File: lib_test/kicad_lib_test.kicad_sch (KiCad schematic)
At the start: 0 parts

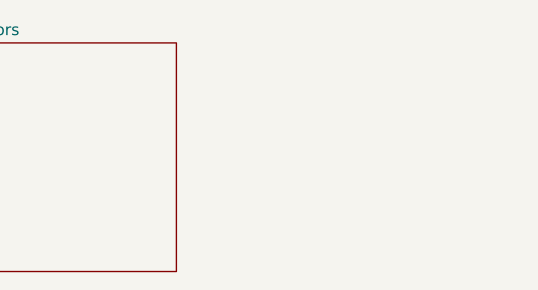
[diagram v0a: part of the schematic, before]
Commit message: add capacitors series to test project
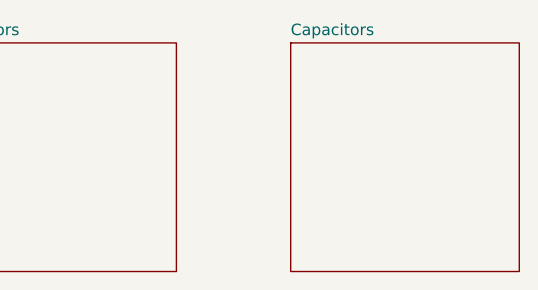
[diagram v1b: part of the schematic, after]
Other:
- added sheet Capacitors (capacitors.kicad_sch)
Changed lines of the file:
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@@
+	)
+	(sheet
+		(at 63.5 25.4)
+		(size 25.4 25.4)
+		(fields_autoplaced yes)
+		(stroke
+			(width 0.1524)
+			(type solid)
+		)
+		(fill
+			(color 0 0 0 0.0000)
+		)
+		(property "Sheetname" "Capacitors"
+			(at 63.5 24.6884 0)
+			(effects
+				(font
+					(size 1.27 1.27)
+				)
+				(justify left bottom)
+			)
+		)
+		(property "Sheetfile" "capacitors.kicad_sch"
+			(at 63.5 51.3846 0)
+			(effects
+				(font
+					(size 1.27 1.27)
+				)
+				(justify left top)
+				(hide yes)
+			)
+		)
+		(instances
+			(project "kicad_lib_test"
+				(path "/032b8f2d-5c08-4381-9e3a-c197ca84e3c5"
+					(page "3")
+				)
+			)
+		)
 	)
 	(sheet

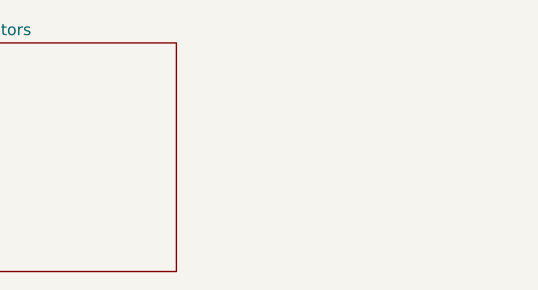
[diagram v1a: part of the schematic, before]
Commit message: add inductor bead 600R, 1.5A, 0.25R
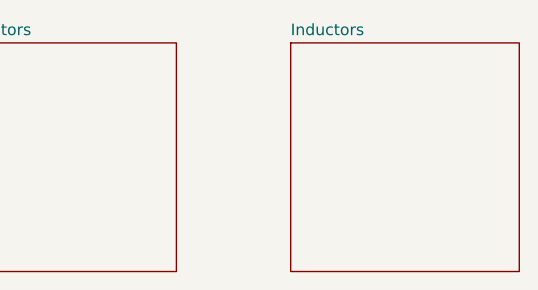
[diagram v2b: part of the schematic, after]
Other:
- added sheet Inductors (inductors.kicad_sch)
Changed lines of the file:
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@@
+		)
+	)
+	(sheet
+		(at 101.6 25.4)
+		(size 25.4 25.4)
+		(fields_autoplaced yes)
+		(stroke
+			(width 0.1524)
+			(type solid)
+		)
+		(fill
+			(color 0 0 0 0.0000)
+		)
+		(property "Sheetname" "Inductors"
+			(at 101.6 24.6884 0)
+			(effects
+				(font
+					(size 1.27 1.27)
+				)
+				(justify left bottom)
+			)
+		)
+		(property "Sheetfile" "inductors.kicad_sch"
+			(at 101.6 51.3846 0)
+			(effects
+				(font
+					(size 1.27 1.27)
+				)
+				(justify left top)
+				(hide yes)
+			)
+		)
+		(instances
+			(project "kicad_lib_test"
+				(path "/032b8f2d-5c08-4381-9e3a-c197ca84e3c5"
+					(page "4")
+				)
+			)
 		)
 	)

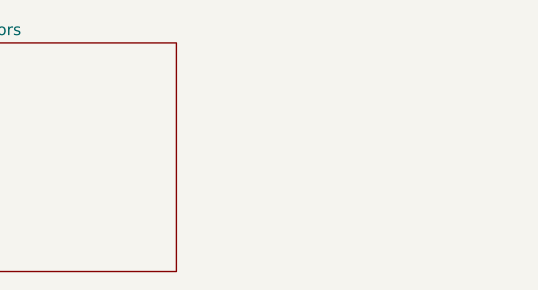
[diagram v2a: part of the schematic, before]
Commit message: add diode tvs uni 2 channel 12V
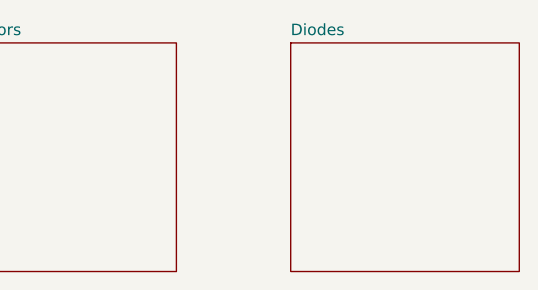
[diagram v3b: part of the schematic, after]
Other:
- added sheet Diodes (diodes.kicad_sch)
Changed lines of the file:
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@@
 	(title_block
 		(title "Lily KiCad Library test")
-		(date "2024-04-17")
+		(date "2024-04-28")
 		(rev "1")
 		(company "LilyTronics")
@@
 				)
 			)
+		)
+	)
+	(sheet
+		(at 139.7 25.4)
+		(size 25.4 25.4)
+		(fields_autoplaced yes)
+		(stroke
+			(width 0.1524)
+			(type solid)
+		)
+		(fill
+			(color 0 0 0 0.0000)
+		)
+		(property "Sheetname" "Diodes"
+			(at 139.7 24.6884 0)
+			(effects
+				(font
+					(size 1.27 1.27)
+				)
+				(justify left bottom)
+			)
+		)
+		(property "Sheetfile" "diodes.kicad_sch"
+			(at 139.7 51.3846 0)
+			(effects
+				(font
+					(size 1.27 1.27)
+				)
+				(justify left top)
+				(hide yes)
+			)
+		)
+		(instances
+			(project "kicad_lib_test"
+				(path "/032b8f2d-5c08-4381-9e3a-c197ca84e3c5"
+					(page "5")
+				)
+			)

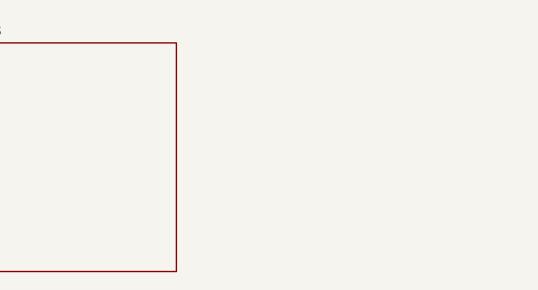
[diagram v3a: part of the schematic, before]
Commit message: add MOSFET AO3400A
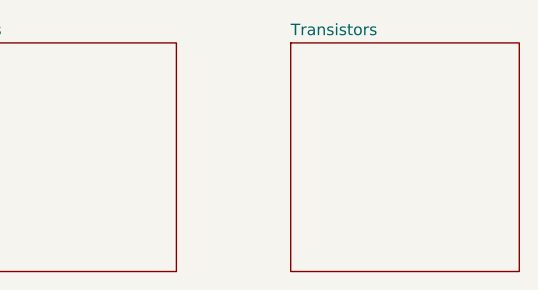
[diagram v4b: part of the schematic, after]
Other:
- added sheet Transistors (transistors.kicad_sch)
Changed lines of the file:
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@@
+	)
+	(sheet
+		(at 177.8 25.4)
+		(size 25.4 25.4)
+		(fields_autoplaced yes)
+		(stroke
+			(width 0.1524)
+			(type solid)
+		)
+		(fill
+			(color 0 0 0 0.0000)
+		)
+		(property "Sheetname" "Transistors"
+			(at 177.8 24.6884 0)
+			(effects
+				(font
+					(size 1.27 1.27)
+				)
+				(justify left bottom)
+			)
+		)
+		(property "Sheetfile" "transistors.kicad_sch"
+			(at 177.8 51.3846 0)
+			(effects
+				(font
+					(size 1.27 1.27)
+				)
+				(justify left top)
+				(hide yes)
+			)
+		)
+		(instances
+			(project "kicad_lib_test"
+				(path "/032b8f2d-5c08-4381-9e3a-c197ca84e3c5"
+					(page "6")
+				)
+			)
+		)
 	)
 	(sheet

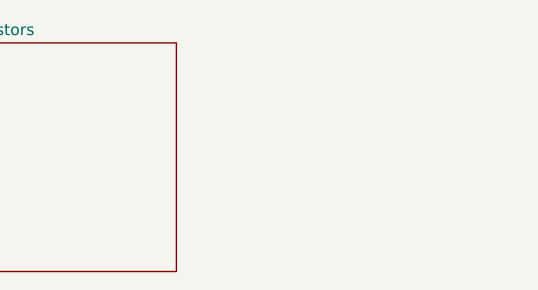
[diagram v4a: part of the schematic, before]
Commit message: add dual opamp TLV272
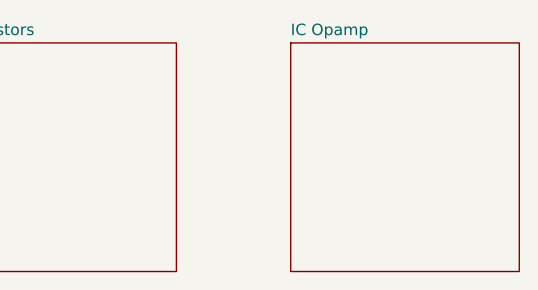
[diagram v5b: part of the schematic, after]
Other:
- added sheet IC Opamp (ic_opamp.kicad_sch)
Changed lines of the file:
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@@
+	)
+	(sheet
+		(at 215.9 25.4)
+		(size 25.4 25.4)
+		(fields_autoplaced yes)
+		(stroke
+			(width 0.1524)
+			(type solid)
+		)
+		(fill
+			(color 0 0 0 0.0000)
+		)
+		(property "Sheetname" "IC Opamp"
+			(at 215.9 24.6884 0)
+			(effects
+				(font
+					(size 1.27 1.27)
+				)
+				(justify left bottom)
+			)
+		)
+		(property "Sheetfile" "ic_opamp.kicad_sch"
+			(at 215.9 51.3846 0)
+			(effects
+				(font
+					(size 1.27 1.27)
+				)
+				(justify left top)
+				(hide yes)
+			)
+		)
+		(instances
+			(project "kicad_lib_test"
+				(path "/032b8f2d-5c08-4381-9e3a-c197ca84e3c5"
+					(page "7")
+				)
+			)
+		)
 	)
 	(sheet

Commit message: add new parts
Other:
- sheet IC Opamp renamed IC Opamps
- added sheet IC Sensors (ic_sensors.kicad_sch)
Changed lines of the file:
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@@
 	)
 	(sheet
-		(at 215.9 25.4)
-		(size 25.4 25.4)
-		(fields_autoplaced yes)
-		(stroke
-			(width 0.1524)
-			(type solid)
-		)
-		(fill
-			(color 0 0 0 0.0000)
-		)
-		(property "Sheetname" "IC Opamp"
-			(at 215.9 24.6884 0)
+		(at 248.92 25.4)
+		(size 25.4 25.4)
+		(fields_autoplaced yes)
+		(stroke
+			(width 0.1524)
+			(type solid)
+		)
+		(fill
+			(color 0 0 0 0.0000)
+		)
+		(property "Sheetname" "IC Sensors"
+			(at 248.92 24.6884 0)
+			(effects
+				(font
+					(size 1.27 1.27)
+				)
+				(justify left bottom)
+			)
+		)
+		(property "Sheetfile" "ic_sensors.kicad_sch"
+			(at 248.92 51.3846 0)
+			(effects
+				(font
+					(size 1.27 1.27)
+				)
+				(justify left top)
+				(hide yes)
+			)
+		)
+		(instances
+			(project "kicad_lib_test"
+				(path "/032b8f2d-5c08-4381-9e3a-c197ca84e3c5"
+					(page "8")
+				)
+			)
+		)
+	)
+	(sheet
+		(at 210.82 25.4)
+		(size 25.4 25.4)
+		(stroke
+			(width 0.1524)
+			(type solid)
+		)
+		(fill
+			(color 0 0 0 0.0000)
+		)
+		(property "Sheetname" "IC Opamps"
+			(at 210.82 24.765 0)
 			(effects
 				(font
@@
 		)
 		(property "Sheetfile" "ic_opamp.kicad_sch"
-			(at 215.9 51.3846 0)
+			(at 210.82 51.3846 0)
 			(effects
 				(font
@@
 	)
 	(sheet
-		(at 63.5 25.4)
+		(at 58.42 25.4)
 		(size 25.4 25.4)
 		(fields_autoplaced yes)
@@
 		)
 		(property "Sheetname" "Capacitors"
-			(at 63.5 24.6884 0)
+			(at 58.42 24.6884 0)
 			(effects
 				(font
@@
 		)
 		(property "Sheetfile" "capacitors.kicad_sch"
-			(at 63.5 51.3846 0)
+			(at 58.42 51.3846 0)
 			(effects
 				(font
@@
 	)
 	(sheet
-		(at 177.8 25.4)
+		(at 172.72 25.4)
 		(size 25.4 25.4)
 		(fields_autoplaced yes)
@@
 		)
 		(property "Sheetname" "Transistors"
-			(at 177.8 24.6884 0)
+			(at 172.72 24.6884 0)
 			(effects
 				(font
@@
 		)
 		(property "Sheetfile" "transistors.kicad_sch"
-			(at 177.8 51.3846 0)
+			(at 172.72 51.3846 0)
 			(effects
 				(font
@@
 	)
 	(sheet
-		(at 25.4 25.4)
+		(at 20.32 25.4)
 		(size 25.4 25.4)
 		(fields_autoplaced yes)
@@
 		)
 		(property "Sheetname" "Resistors"
-			(at 25.4 24.6884 0)
+			(at 20.32 24.6884 0)
 			(effects
 				(font
@@
 		)
 		(property "Sheetfile" "resistors.kicad_sch"
-			(at 25.4 51.3846 0)
+			(at 20.32 51.3846 0)
 			(effects
 				(font
@@
 	)
 	(sheet
-		(at 101.6 25.4)
+		(at 96.52 25.4)
 		(size 25.4 25.4)
 		(fields_autoplaced yes)
@@
 		)
 		(property "Sheetname" "Inductors"
-			(at 101.6 24.6884 0)
+			(at 96.52 24.6884 0)
 			(effects
 				(font
@@
 		)
 		(property "Sheetfile" "inductors.kicad_sch"
-			(at 101.6 51.3846 0)
+			(at 96.52 51.3846 0)
 			(effects
 				(font
@@
 	)
 	(sheet
-		(at 139.7 25.4)
+		(at 134.62 25.4)
 		(size 25.4 25.4)
 		(fields_autoplaced yes)
@@
 		)
 		(property "Sheetname" "Diodes"
-			(at 139.7 24.6884 0)
+			(at 134.62 24.6884 0)
 			(effects
 				(font
@@
 		)
 		(property "Sheetfile" "diodes.kicad_sch"
-			(at 139.7 51.3846 0)
-			(effects
-				(font
+			(at 134.62 51.3846 0)
+			(effects
+				(font

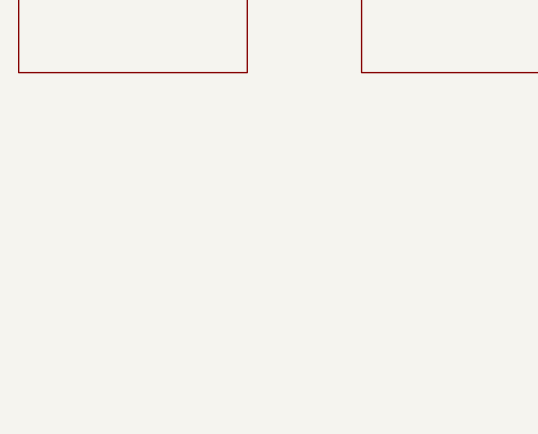
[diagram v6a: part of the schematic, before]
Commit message: add LM393
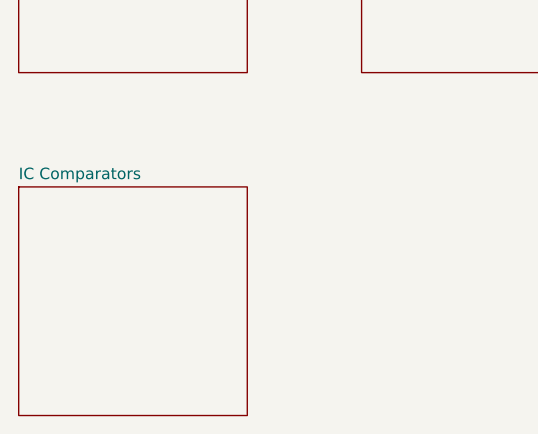
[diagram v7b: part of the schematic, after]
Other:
- added sheet IC Comparators (ic_comparators.kicad_sch)
- sheet IC Opamps: file ic_opamp.kicad_sch -> ic_opamps.kicad_sch
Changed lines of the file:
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@@
 	(title_block
 		(title "Lily KiCad Library test")
-		(date "2024-04-28")
+		(date "2024-05-03")
 		(rev "1")
 		(company "LilyTronics")
@@
 			)
 		)
-		(property "Sheetfile" "ic_opamp.kicad_sch"
+		(property "Sheetfile" "ic_opamps.kicad_sch"
 			(at 210.82 51.3846 0)
 			(effects
@@
 				)
 			)
+		)
+	)
+	(sheet
+		(at 20.32 63.5)
+		(size 25.4 25.4)
+		(fields_autoplaced yes)
+		(stroke
+			(width 0.1524)
+			(type solid)
+		)
+		(fill
+			(color 0 0 0 0.0000)
+		)
+		(property "Sheetname" "IC Comparators"
+			(at 20.32 62.7884 0)
+			(effects
+				(font
+					(size 1.27 1.27)
+				)
+				(justify left bottom)
+			)
+		)
+		(property "Sheetfile" "ic_comparators.kicad_sch"
+			(at 20.32 89.4846 0)
+			(effects
+				(font
+					(size 1.27 1.27)
+				)
+				(justify left top)
+				(hide yes)
+			)
+		)
+		(instances
+			(project "kicad_lib_test"
+				(path "/032b8f2d-5c08-4381-9e3a-c197ca84e3c5"
+					(page "9")
+				)
+			)

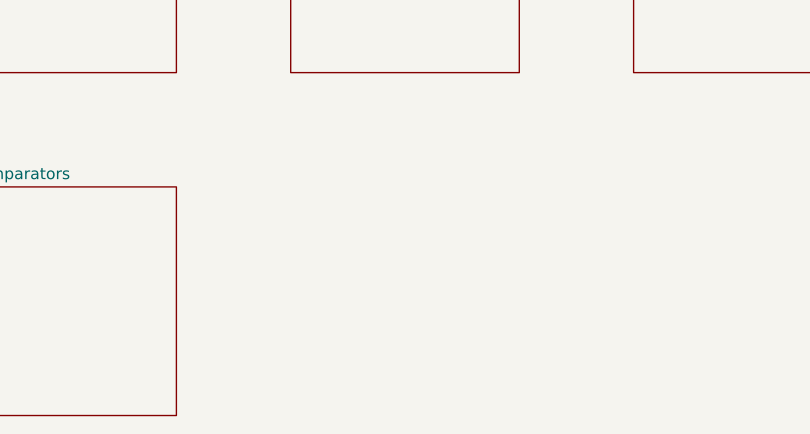
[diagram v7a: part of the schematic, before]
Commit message: add DIN41612 connector
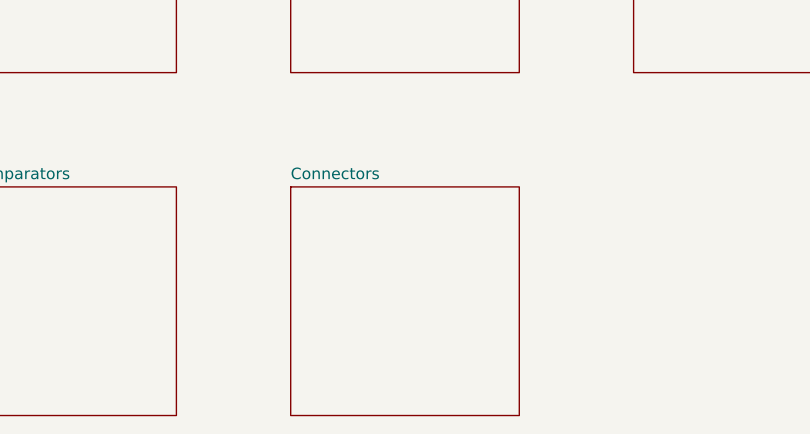
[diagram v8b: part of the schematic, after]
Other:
- added sheet Connectors (connectors.kicad_sch)
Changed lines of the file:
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@@
+	)
+	(sheet
+		(at 58.42 63.5)
+		(size 25.4 25.4)
+		(fields_autoplaced yes)
+		(stroke
+			(width 0.1524)
+			(type solid)
+		)
+		(fill
+			(color 0 0 0 0.0000)
+		)
+		(property "Sheetname" "Connectors"
+			(at 58.42 62.7884 0)
+			(effects
+				(font
+					(size 1.27 1.27)
+				)
+				(justify left bottom)
+			)
+		)
+		(property "Sheetfile" "connectors.kicad_sch"
+			(at 58.42 89.4846 0)
+			(effects
+				(font
+					(size 1.27 1.27)
+				)
+				(justify left top)
+				(hide yes)
+			)
+		)
+		(instances
+			(project "kicad_lib_test"
+				(path "/032b8f2d-5c08-4381-9e3a-c197ca84e3c5"
+					(page "10")
+				)
+			)
+		)
 	)
 	(sheet
